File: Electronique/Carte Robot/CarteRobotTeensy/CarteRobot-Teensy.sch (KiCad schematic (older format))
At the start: 37 parts, among them J1 Conn_Bat2, J10 Conn_01x03, J11 Conn_01x05, J12 Conn_01x05, J13 Conn_01x04, J14 Conn_02x04_Counter_Clockwise, J15 Shield-Actionneurs, J19 Conn_IHM, J2 Conn_Bat1, J3 Conn_OnOff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

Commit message: passage Teensy 3.5 + debut lidar
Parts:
- removed R6, R7: 390k, symbol Device:R
- J5: value Teensy-3.6 -> Teensy-3.5; footprint Mes_empreintes:Teensy-3.6 -> Mes_empreintes:Teensy-3.5-3.6; symbol Mes_symboles:Teensy-3.6 -> Mes_symboles:Teensy-3.5-3.6
- R4, R5, R8, R9: footprint (none) -> Resistor_SMD:R_0805_2012Metric_Pad1.20x1.40mm_HandSolder
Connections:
- net labels added: 17
- wire segments 220 -> 222
- no-connect marks 12 -> 11
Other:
- moved on the sheet: J11, J12, R8, R9

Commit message: nouvelles pieces lidar
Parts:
- R4, R5, R8, R9: footprint Resistor_SMD:R_0805_2012Metric_Pad1.20x1.40mm_HandSolder -> Resistor_THT:R_Axial_DIN0207_L6.3mm_D2.5mm_P10.16mm_Horizontal
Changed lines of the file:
@@
 F 0 "R8" H 9250 4150 50  0000 L CNN
 F 1 "390k" H 9250 4250 50  0000 L CNN
-F 2 "Resistor_SMD:R_0805_2012Metric_Pad1.20x1.40mm_HandSolder" V 9130 4200 50  0001 C CNN
+F 2 "Resistor_THT:R_Axial_DIN0207_L6.3mm_D2.5mm_P10.16mm_Horizontal" V 9130 4200 50  0001 C CNN
 F 3 "~" H 9200 4200 50  0001 C CNN
 	1    9200 4200
@@
 F 0 "R9" H 9600 4150 50  0000 L CNN
 F 1 "390k" H 9600 4250 50  0000 L CNN
-F 2 "Resistor_SMD:R_0805_2012Metric_Pad1.20x1.40mm_HandSolder" V 9480 4200 50  0001 C CNN
+F 2 "Resistor_THT:R_Axial_DIN0207_L6.3mm_D2.5mm_P10.16mm_Horizontal" V 9480 4200 50  0001 C CNN
 F 3 "~" H 9550 4200 50  0001 C CNN
 	1    9550 4200
@@
 F 0 "R4" H 9250 4900 50  0000 L CNN
 F 1 "390k" H 9250 5000 50  0000 L CNN
-F 2 "Resistor_SMD:R_0805_2012Metric_Pad1.20x1.40mm_HandSolder" V 9130 4950 50  0001 C CNN
+F 2 "Resistor_THT:R_Axial_DIN0207_L6.3mm_D2.5mm_P10.16mm_Horizontal" V 9130 4950 50  0001 C CNN
 F 3 "~" H 9200 4950 50  0001 C CNN
 	1    9200 4950
@@
 F 0 "R5" H 9600 4900 50  0000 L CNN
 F 1 "390k" H 9600 5000 50  0000 L CNN
-F 2 "Resistor_SMD:R_0805_2012Metric_Pad1.20x1.40mm_HandSolder" V 9480 4950 50  0001 C CNN
+F 2 "Resistor_THT:R_Axial_DIN0207_L6.3mm_D2.5mm_P10.16mm_Horizontal" V 9480 4950 50  0001 C CNN
 F 3 "~" H 9550 4950 50  0001 C CNN
 	1    9550 4950

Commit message: modif elec + meca
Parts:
- added C3: 10u, Capacitor_THT:CP_Radial_D5.0mm_P2.00mm, symbol Device:CP1
- added J16, J17, J18, J20, J21: Conn_Aru, Connector_Molex:Molex_KK-254_AE-6410-02A_1x02_P2.54mm_Vertical, symbol Connector_Generic:Conn_01x02
- added R10, R11, R6, R7: 1k, Resistor_THT:R_Axial_DIN0207_L6.3mm_D2.5mm_P10.16mm_Horizontal, symbol Device:R
- added R12, R13: 4.7k, Resistor_THT:R_Axial_DIN0207_L6.3mm_D2.5mm_P10.16mm_Horizontal, symbol Device:R
- C1, C2: footprint Capacitor_THT:CP_Radial_D6.3mm_P2.50mm -> Capacitor_THT:CP_Radial_D5.0mm_P2.50mm
- J15: footprint Mes_empreintes:Adaptateur-Servo-Dynamixel -> Mes_empreintes:Shield-Actionneurs
- J6, J7: footprint Connector_Molex:Molex_KK-254_AE-6410-04A_1x04_P2.54mm_Vertical -> Connector_JST:JST_XH_B4B-XH-A_1x04_P2.50mm_Vertical
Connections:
- net +3V3: now also C3.1, R12.1, R13.1
- net +5V: now also J21.1 (Pin_1), R10.1, R11.1, R6.1, R7.1
- net CE: now also J5.20 (28); no longer J5.22 (30)
- net CODD_A: now also J5.22 (30); no longer J5.21 (29)
- net CODD_B: now also J5.21 (29); no longer J5.20 (28)
- net GND: now also J15.4, C3.2, J16.1 (Pin_1), J17.1 (Pin_1), J18.1 (Pin_1), J20.1 (Pin_1); no longer J15.5
- net MS1: now also J16.2 (Pin_2), R6.2
- net MS2: now also J18.2 (Pin_2), R7.2
- net MS3: now also J17.2 (Pin_2), R10.2
- net MS4: now also J20.2 (Pin_2), R11.2
- net RX3: now also J15.5; no longer J15.3
- net SCL2: now also J15.1, R13.2
- net SDA2: now also J15.2, R12.2
- net TX3: now also J15.6; no longer J15.4
- net Varu: now also J15.3; no longer J15.2
- net Tirette: now reaches J5.44 (22)
- net Tirette: now also J21.2 (Pin_2)
- no-connect marks 11 -> 10
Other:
- moved on the sheet: J14

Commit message: creation projet sur platformIO
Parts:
- R4, R5, R8, R9: value 390k -> 4.7k
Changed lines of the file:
@@
 P 9200 4200
 F 0 "R8" H 9250 4150 50  0000 L CNN
-F 1 "390k" H 9250 4250 50  0000 L CNN
+F 1 "4.7k" H 9250 4250 50  0000 L CNN
 F 2 "Resistor_THT:R_Axial_DIN0207_L6.3mm_D2.5mm_P10.16mm_Horizontal" V 9130 4200 50  0001 C CNN
 F 3 "~" H 9200 4200 50  0001 C CNN
@@
 P 9550 4200
 F 0 "R9" H 9600 4150 50  0000 L CNN
-F 1 "390k" H 9600 4250 50  0000 L CNN
+F 1 "4.7k" H 9600 4250 50  0000 L CNN
 F 2 "Resistor_THT:R_Axial_DIN0207_L6.3mm_D2.5mm_P10.16mm_Horizontal" V 9480 4200 50  0001 C CNN
 F 3 "~" H 9550 4200 50  0001 C CNN
@@
 P 9200 4950
 F 0 "R4" H 9250 4900 50  0000 L CNN
-F 1 "390k" H 9250 5000 50  0000 L CNN
+F 1 "4.7k" H 9250 5000 50  0000 L CNN
 F 2 "Resistor_THT:R_Axial_DIN0207_L6.3mm_D2.5mm_P10.16mm_Horizontal" V 9130 4950 50  0001 C CNN
 F 3 "~" H 9200 4950 50  0001 C CNN
@@
 P 9550 4950
 F 0 "R5" H 9600 4900 50  0000 L CNN
-F 1 "390k" H 9600 5000 50  0000 L CNN
+F 1 "4.7k" H 9600 5000 50  0000 L CNN
 F 2 "Resistor_THT:R_Axial_DIN0207_L6.3mm_D2.5mm_P10.16mm_Horizontal" V 9480 4950 50  0001 C CNN
 F 3 "~" H 9550 4950 50  0001 C CNN

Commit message: routage pcb
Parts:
- added C4: 0,33u, Capacitor_THT:CP_Radial_D5.0mm_P2.00mm, symbol Device:CP1
- added C5: 0,1u, Capacitor_THT:CP_Radial_D5.0mm_P2.00mm, symbol Device:CP1
- added D3: LED, LED_THT:LED_D5.0mm_Clear, symbol Device:LED
- added J22: Conn_01x03, Connector_PinHeader_2.54mm:PinHeader_1x03_P2.54mm_Vertical, symbol Connector_Generic:Conn_01x03
- added R14: 500, Resistor_THT:R_Axial_DIN0207_L6.3mm_D2.5mm_P10.16mm_Horizontal, symbol Device:R
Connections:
- net +3V3: now also J22.1 (Pin_1)
- net +5V: now also J19.4 (Pin_4), C5.1
- net GND: now also C4.2, C5.2, D3.1 (K), J22.3 (Pin_3)
- net RX4: now also J19.2 (Pin_2); no longer J19.3 (Pin_3)
- net TX4: now also J19.3 (Pin_3); no longer J19.2 (Pin_2)
- net Von: now also C4.1; no longer J19.4 (Pin_4)
- net LED: now reaches J5.4 (2)
- net LED: now also R14.1
- net STRAT: now reaches J5.7 (5)
- net STRAT: now also J22.2 (Pin_2)
- new net: D3.2 (A), R14.2
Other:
- moved on the sheet: H1, H2, H3, H4, J13, J19, J21, U1

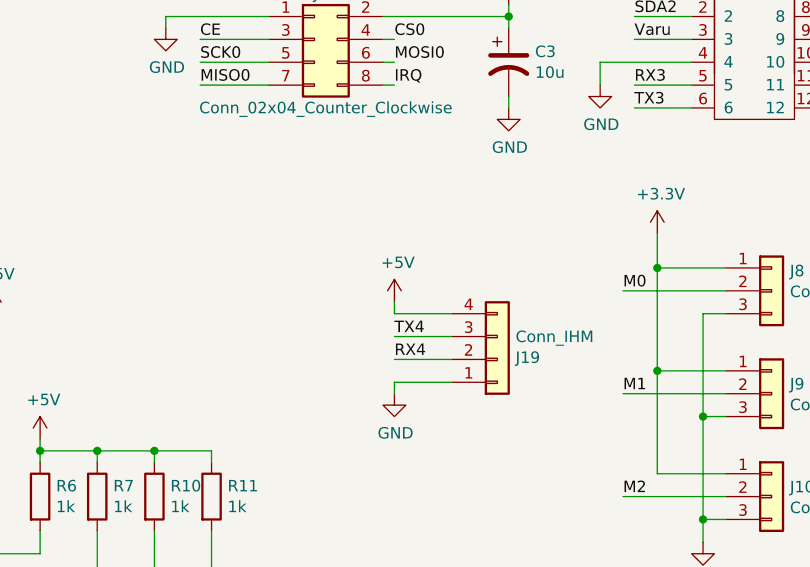
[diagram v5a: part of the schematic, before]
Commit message: correction carte elec
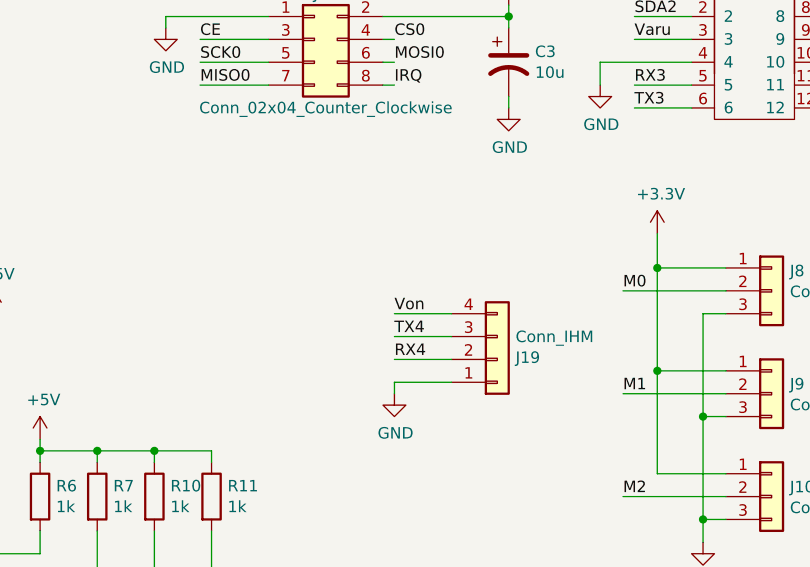
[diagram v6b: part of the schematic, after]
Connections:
- net +5V: no longer J19.4 (Pin_4)
- net Von: now also J19.4 (Pin_4)
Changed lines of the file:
@@
 	3150 4100 3300 4100
-Wire Wire Line
-	8850 2300 8600 2300
-Wire Wire Line
-	8600 2300 8600 2250
-$Comp
-L power:+5V #PWR0117
-U 1 1 614DFAA8
-P 8600 2250
-F 0 "#PWR0117" H 8600 2100 50  0001 C CNN
-F 1 "+5V" H 8615 2423 50  0000 C CNN
-F 2 "" H 8600 2250 50  0001 C CNN
-F 3 "" H 8600 2250 50  0001 C CNN
-	1    8600 2250
-	1    0    0    -1
-$EndComp
 Wire Wire Line
 	5100 3050 5400 3050
@@
 	5100 2950 5400 2950
 NoConn ~ 5100 3050
+Wire Wire Line
+	8850 2300 8600 2300
+Text Label 8600 2300 0    50   ~ 0
+Von
 $EndSCHEMATC
